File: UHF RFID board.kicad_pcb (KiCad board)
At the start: 2 copper layers, 67.3 x 36.7 mm, 45 parts, among them J1 FZ_full_module, J2 picoblade, J3 SPI, J4 ICSP, U1 YRM1001, U2 SEC1210

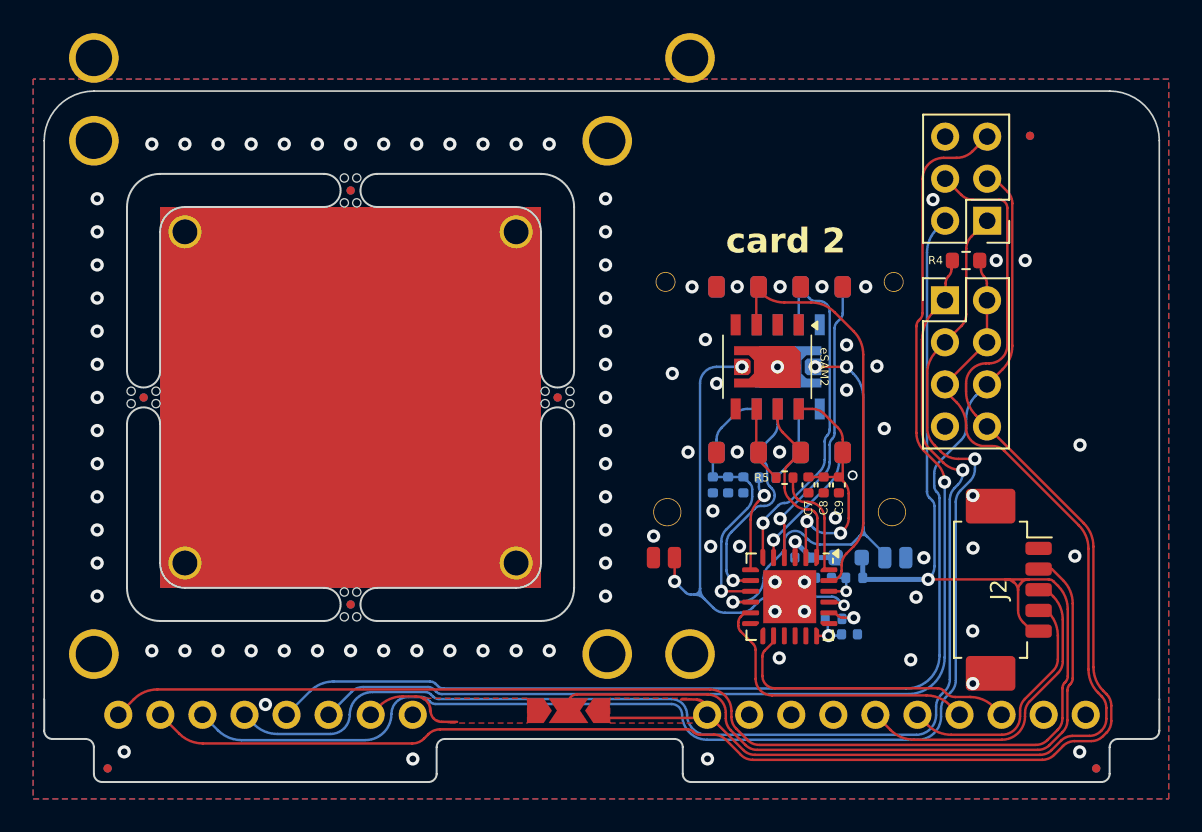
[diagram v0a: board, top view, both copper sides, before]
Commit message: V2.5.2 production update
- removed unused + out-of-bounds mounting holes for the yrm1003 module that could throw errors in fab houses
- corrected SIMMP-00801B000-G sim slot footprint, fab outline was bigger than the part, and model was not accurate for the part.
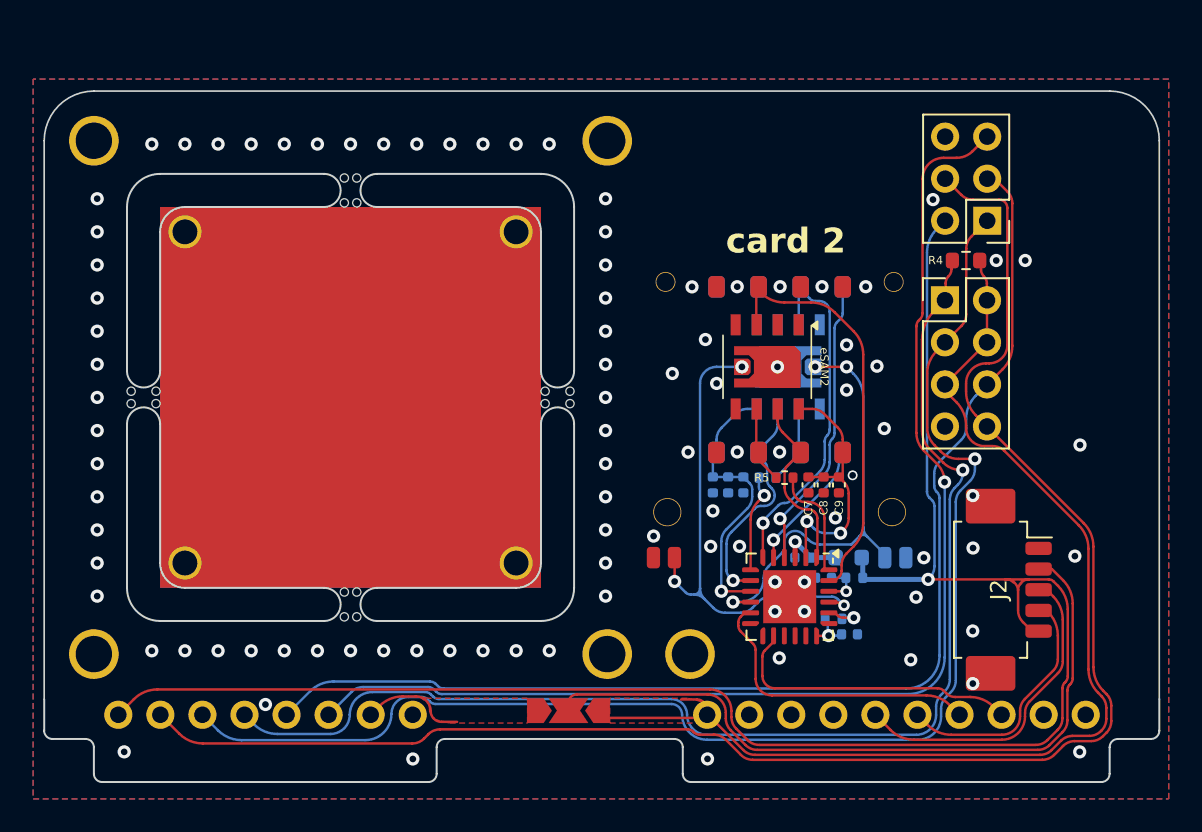
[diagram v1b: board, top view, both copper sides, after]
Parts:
- removed ? (x9): , 
- removed REF** (x5): Fiducial_0.5mm_Mask1mm, Fiducial:Fiducial_0.5mm_Mask1mm
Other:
- board text added: "UHF | RFID | SAM Version 2.5.2"
- board text removed: "UHF | RFID | SAM Version 2.5"

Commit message: V2.5.3 yrm footprint center pad corner rounding
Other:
- board text added: "UHF | RFID | SAM Version 2.5.3"
- board text removed: "UHF | RFID | SAM Version 2.5.2"
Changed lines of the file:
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@@
 	(net 50 "unconnected-(SAM2-VPP-Pad6)")
 	(net 51 "unconnected-(SAM2-C8-Pad8)")
-	(net 52 "unconnected-(U1-center_pad_area-Pad6)")
-	(net 53 "unconnected-(U1-center_pad_area-Pad6)_0")
-	(net 54 "unconnected-(U1-center_pad_area-Pad6)_1")
-	(net 55 "unconnected-(U1-center_pad_area-Pad6)_2")
-	(net 56 "unconnected-(U1-center_pad_area-Pad6)_3")
-	(net 57 "unconnected-(U1-center_pad_area-Pad6)_4")
+	(net 52 "unconnected-(U1-center_pad_area-Pad6)_2")
 	(footprint "Logos:[UHF RFID for Flipper] repo by Frux"
 		(layer "F.Cu")
@@
 			)
 		)
-		(sheetname "Root")
-		(sheetfile "UHF RFID board.kicad_sch")
 		(attr dnp)
 		(fp_circle
@@
 			)
 		)
-		(fp_text user "35^2 x 25^2"
-			(at 15.5 26.5 -90)
+		(fp_text user "40^2 x 35^2"
+			(at 20.5 26.5 -90)
 			(unlocked yes)
 			(layer "Eco2.User")
@@
 			)
 		)
-		(fp_text user "40^2 x 35^2"
-			(at 20.5 26.5 -90)
+		(fp_text user "35^2 x 25^2"
+			(at 15.5 26.5 -90)
 			(unlocked yes)
 			(layer "Eco2.User")
@@
 			(layers "*.Cu")
 			(remove_unused_layers no)
-			(net 55 "unconnected-(U1-center_pad_area-Pad6)_2")
+			(net 52 "unconnected-(U1-center_pad_area-Pad6)_2")
 			(pinfunction "center_pad_area")
 			(pintype "input+no_connect")
@@
 			(layers "*.Cu")
 			(remove_unused_layers no)
-			(net 57 "unconnected-(U1-center_pad_area-Pad6)_4")
+			(net 52 "unconnected-(U1-center_pad_area-Pad6)_2")
 			(pinfunction "center_pad_area")
 			(pintype "input+no_connect")
 		)
-		(pad "6" smd rect
-			(at 0 0 270)
+		(pad "6" smd roundrect
+			(at 0 0)
 			(size 23 23)
 			(layers "F.Cu")
-			(net 53 "unconnected-(U1-center_pad_area-Pad6)_0")
+			(roundrect_rratio 0.0652173913)
+			(net 52 "unconnected-(U1-center_pad_area-Pad6)_2")
 			(pinfunction "center_pad_area")
 			(pintype "input+no_connect")
 		)
-		(pad "6" smd rect
+		(pad "6" smd roundrect
 			(at 0 0 90)
 			(size 23 23)
 			(layers "B.Cu")
-			(net 54 "unconnected-(U1-center_pad_area-Pad6)_1")
+			(roundrect_rratio 0.0652173913)
+			(net 52 "unconnected-(U1-center_pad_area-Pad6)_2")
 			(pinfunction "center_pad_area")
 			(pintype "input+no_connect")
@@
 			(layers "*.Cu")
 			(remove_unused_layers no)
-			(net 56 "unconnected-(U1-center_pad_area-Pad6)_3")
+			(net 52 "unconnected-(U1-center_pad_area-Pad6)_2")
 			(pinfunction "center_pad_area")
 			(pintype "input+no_connect")
@@
 			(layers "*.Cu")
 			(remove_unused_layers no)
-			(net 52 "unconnected-(U1-center_pad_area-Pad6)")
+			(net 52 "unconnected-(U1-center_pad_area-Pad6)_2")
 			(pinfunction "center_pad_area")
 			(pintype "input+no_connect")
@@
 		)
 	)
-	(gr_text "UHF | RFID | SAM\nVersion 2.5.2"
+	(gr_text "UHF | RFID | SAM\nVersion 2.5.3"
 		(at 154.89 100.6 0)
 		(layer "F.Mask")
@@
 			(justify left)
 		)
-		(render_cache "UHF | RFID | SAM\nVersion 2.5.2" 0
+		(render_cache "UHF | RFID | SAM\nVersion 2.5.3" 0
 			(polygon
 				(pts
@@
 			(polygon
 				(pts
-					(xy 165.696769 101.855) (xy 165.171891 101.855) (xy 165.171891 101.456151) (xy 165.182633 101.406348)
-					(xy 165.20584 101.373597) (xy 165.248284 101.34575) (xy 165.287173 101.339159) (xy 165.637418 101.339159)
-					(xy 165.637418 101.057791) (xy 165.22538 101.057791) (xy 165.184103 101.041915) (xy 165.167739 101.00308)
-					(xy 165.184103 100.96449) (xy 165.22538 100.94837) (xy 165.637662 100.94837) (xy 165.687387 100.95888)
-					(xy 165.719972 100.981587) (xy 165.747818 101.022932) (xy 165.75441 101.060966) (xy 165.75441 101.334762)
-					(xy 165.743513 101.383783) (xy 165.719972 101.415607) (xy 165.677098 101.442268) (xy 165.637662 101.448579)
-					(xy 165.287173 101.448579) (xy 165.287173 101.745579) (xy 165.696769 101.745579) (xy 165.737069 101.761699)
-					(xy 165.75441 101.800289) (xy 165.737069 101.839124)
+					(xy 165.75441 101.061699) (xy 165.75441 101.273946) (xy 165.747815 101.3255) (xy 165.725788 101.372436)
+					(xy 165.707515 101.393869) (xy 165.736836 101.435726) (xy 165.753329 101.484172) (xy 165.755631 101.511594)
+					(xy 165.755631 101.73874) (xy 165.744735 101.788148) (xy 165.721193 101.820806) (xy 165.67832 101.848455)
+					(xy 165.638883 101.855) (xy 165.230753 101.855) (xy 165.189965 101.839124) (xy 165.173112 101.800289)
+					(xy 165.189965 101.761699) (xy 165.230753 101.745579) (xy 165.637418 101.745579) (xy 165.637418 101.510373)
+					(xy 165.620565 101.466898) (xy 165.579776 101.448579) (xy 165.347501 101.448579) (xy 165.306713 101.432948)
+					(xy 165.28986 101.393869) (xy 165.306713 101.355279) (xy 165.347501 101.339159) (xy 165.581242 101.339159)
+					(xy 165.621542 101.322306) (xy 165.638883 101.281273) (xy 165.638883 101.057791) (xy 165.226601 101.057791)
+					(xy 165.185812 101.041915) (xy 165.16896 101.00308) (xy 165.185812 100.96449) (xy 165.226601 100.94837)
+					(xy 165.638883 100.94837) (xy 165.688454 100.958957) (xy 165.720704 100.981831) (xy 165.747958 101.023451)
 				)
 			)

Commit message: Version 2.5.4 - copper to board edge fix
copper to board edge clearance was erroneously set to 0 instead of .254mm . PCB still functioned fine, this is purely to aid manufacturing and prevent manufacturers from throwing errors at you.
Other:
- board text added: "UHF | RFID | SAM Version 2.5.4"
- board text removed: "UHF | RFID | SAM Version 2.5.3"
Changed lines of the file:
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@@
 		)
 	)
-	(gr_text "UHF | RFID | SAM\nVersion 2.5.3"
+	(gr_text "UHF | RFID | SAM\nVersion 2.5.4"
 		(at 154.89 100.6 0)
 		(layer "F.Mask")
@@
 			(justify left)
 		)
-		(render_cache "UHF | RFID | SAM\nVersion 2.5.3" 0
+		(render_cache "UHF | RFID | SAM\nVersion 2.5.4" 0
 			(polygon
 				(pts
@@
 			(polygon
 				(pts
-					(xy 165.75441 101.061699) (xy 165.75441 101.273946) (xy 165.747815 101.3255) (xy 165.725788 101.372436)
-					(xy 165.707515 101.393869) (xy 165.736836 101.435726) (xy 165.753329 101.484172) (xy 165.755631 101.511594)
-					(xy 165.755631 101.73874) (xy 165.744735 101.788148) (xy 165.721193 101.820806) (xy 165.67832 101.848455)
-					(xy 165.638883 101.855) (xy 165.230753 101.855) (xy 165.189965 101.839124) (xy 165.173112 101.800289)
-					(xy 165.189965 101.761699) (xy 165.230753 101.745579) (xy 165.637418 101.745579) (xy 165.637418 101.510373)
-					(xy 165.620565 101.466898) (xy 165.579776 101.448579) (xy 165.347501 101.448579) (xy 165.306713 101.432948)
-					(xy 165.28986 101.393869) (xy 165.306713 101.355279) (xy 165.347501 101.339159) (xy 165.581242 101.339159)
-					(xy 165.621542 101.322306) (xy 165.638883 101.281273) (xy 165.638883 101.057791) (xy 165.226601 101.057791)
-					(xy 165.185812 101.041915) (xy 165.16896 101.00308) (xy 165.185812 100.96449) (xy 165.226601 100.94837)
-					(xy 165.638883 100.94837) (xy 165.688454 100.958957) (xy 165.720704 100.981831) (xy 165.747958 101.023451)
-				)
-			)
+					(xy 165.550223 101.797602) (xy 165.550223 101.558) (xy 165.202665 101.558) (xy 165.202665 101.006988)
+					(xy 165.220006 100.965711) (xy 165.261772 100.94837) (xy 165.302072 100.965956) (xy 165.319413 101.007721)
+					(xy 165.319413 101.448579) (xy 165.550223 101.448579) (xy 165.550223 101.102732) (xy 165.567076 101.060233)
+					(xy 165.607864 101.042159) (xy 165.648897 101.060233) (xy 165.66575 101.102732) (xy 165.66575 101.448579)
+					(xy 165.706538 101.464699) (xy 165.723391 101.50329) (xy 165.706538 101.542124) (xy 165.66575 101.558)
+					(xy 165.66575 101.797847) (xy 165.648408 101.838391) (xy 165.607864 101.855) (xy 165.567076 101.838391)
+				)
+			)

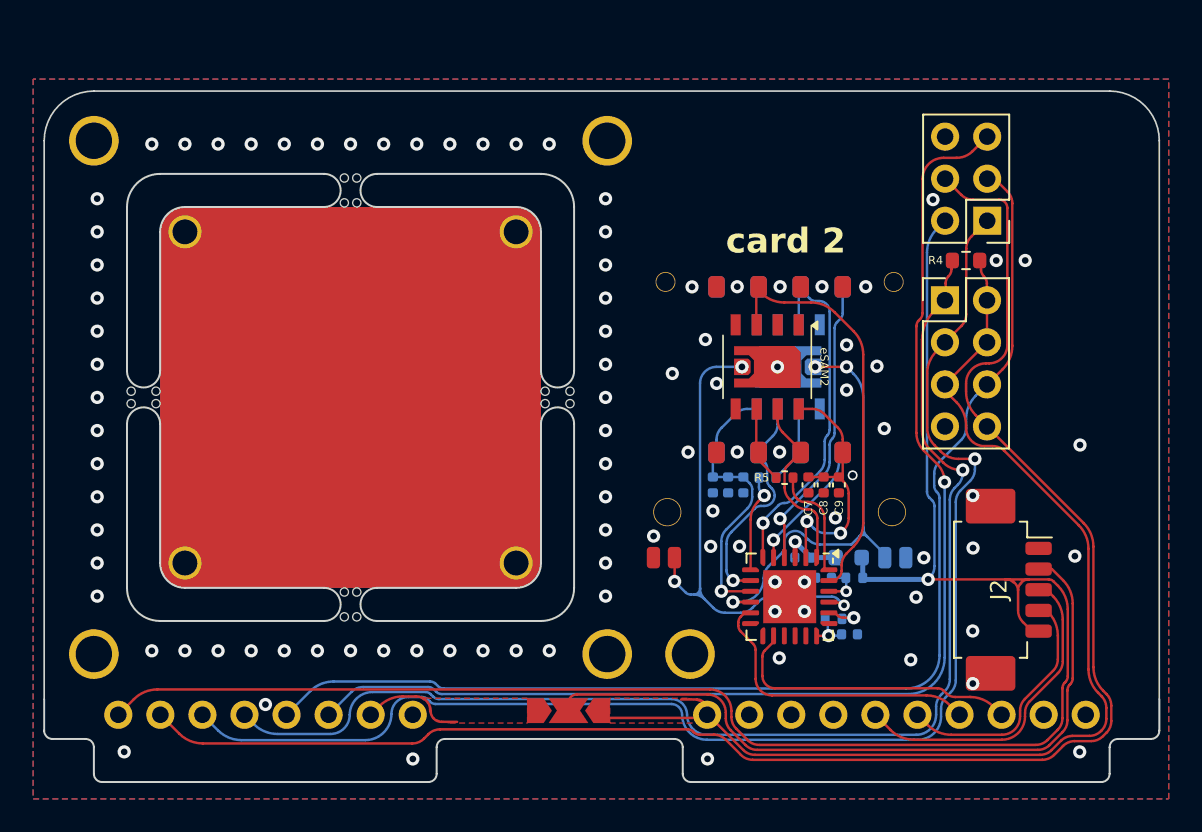
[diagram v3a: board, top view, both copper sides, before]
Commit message: V2.6.0
- flipped the inputs of the picoblade connector, so there's no longer a need for a pass-through cable which in hindsight, good. it seemed dumb a long time ago, but you live and learn. Now the off-the shelf cable from Molex (P/N: 151340500) will work as-is, no rewiring needed.
- nudged the whole SAM stuff 1mm higher, which should no longer hinder connecting/disconnecting the picoblade cable in some cases.
(previously if a SIM slot was soldered in CARD 2, the connector would barely hit the end of the SIM slot. Now it doesn't.)
- updated board version number to V2.6.0
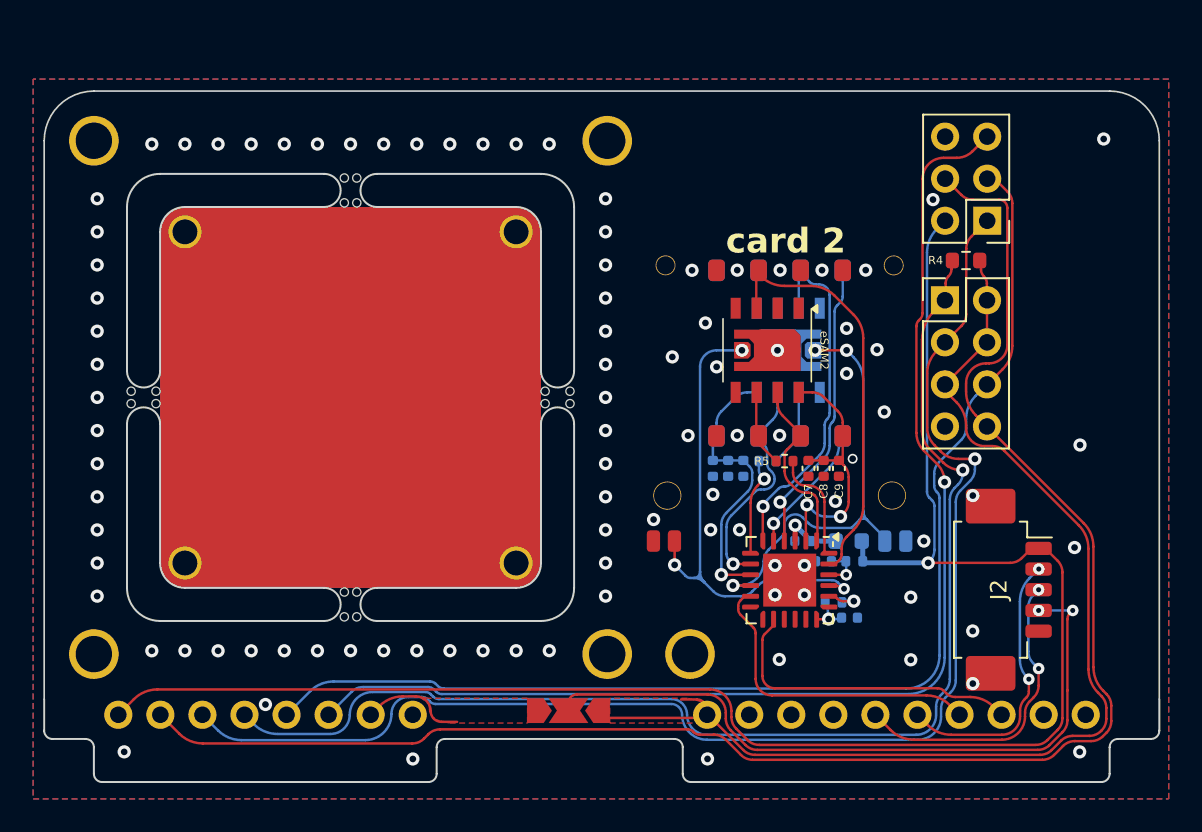
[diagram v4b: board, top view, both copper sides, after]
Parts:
- moved C1 1.00 mm to (167.0, 127.4)
- moved C2 1.00 mm to (165.4, 124.0)
- moved C3 1.00 mm to (164.2, 122.8)
- moved C4 1.00 mm to (160.6, 118.4)
- moved C5 1.00 mm to (159.7, 118.4)
- moved C6 1.00 mm to (158.8, 118.4)
- moved C7 1.00 mm to (164.5, 118.4)
- moved C8 1.00 mm to (165.4, 118.4)
- moved C9 1.00 mm to (166.4, 118.4)
- moved L1 1.00 mm to (166.9, 122.8)
- moved R1 1.00 mm to (166.0, 126.5)
- moved R2 1.00 mm to (167.3, 124.0)
- moved R3 1.00 mm to (162.0, 117.9)
- moved R5 1.00 mm to (163.1, 117.9)
- moved SAM1 1.00 mm to (159.0, 116.4)
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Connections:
- J2 pad 1: GND -> +5V
- J2 pad 2: /EN -> /UART_RX
- J2 pad 4: /UART_RX -> /EN
- J2 pad 5: +5V -> GND
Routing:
- net +5V: track 109.2 -> 104.2 mm
- net /UART_RX: track 15.1 -> 16.8 mm, vias 0 -> 2
- net /EN: track 44.1 -> 42.4 mm, vias 0 -> 2
- net /PC1: track 18.1 -> 19.1 mm
- net /PC0: track 18.0 -> 19.0 mm
- net /UART_TX: track 19.6 -> 18.6 mm, vias 0 -> 2
- net GND: vias 96 -> 94
- removed copper zone on F.Cu, net +5V
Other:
- board text added: "UHF | RFID | SAM Version 2.6.0"
- board text removed: "UHF | RFID | SAM Version 2.5.4"
